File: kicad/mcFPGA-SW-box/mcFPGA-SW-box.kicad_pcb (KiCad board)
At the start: 4 copper layers, 120 parts, among them J1 Conn_01x04, J10 Conn_01x02, J11 Conn_01x02, J12 Conn_01x02, J2 Conn_01x04, J3 Conn_01x04, J4 Conn_01x04, J5 Conn_01x04, J6 Conn_01x04, J7 Conn_01x04, J8 Conn_01x02, J9 Conn_01x04, U1 74HC595, U10 NC7SB3157P6X, U11 NC7SB3157P6X, U12 NC7SB3157P6X, U13 NC7SB3157P6X, U14 NC7SB3157P6X, U15 NC7SB3157P6X, U16 NC7SB3157P6X, U17 NC7SB3157P6X, U18 NC7SB3157P6X, U19 NC7SB3157P6X, U2 74HC595, U20 NC7SB3157P6X, U21 NC7SB3157P6X, U22 NC7SB3157P6X, U23 NC7SB3157P6X, U24 NC7SB3157P6X, U25 NC7SB3157P6X, U26 NC7SB3157P6X, U27 NC7SB3157P6X, U28 NC7SB3157P6X, U29 NC7SB3157P6X, U3 74HC595, U30 NC7SB3157P6X, U31 NC7SB3157P6X, U32 NC7SB3157P6X, U33 NC7SB3157P6X, U34 NC7SB3157P6X, U35 NC7SB3157P6X, U36 NC7SB3157P6X, U4 74HC595, U5 NC7SB3157P6X, U6 NC7SB3157P6X, U7 NC7SB3157P6X, U8 NC7SB3157P6X, U9 NC7SB3157P6X

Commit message: start layout of SW box
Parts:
- moved D25 240.0 mm to (114.3, 88.9)
- moved D26 238.8 mm to (114.3, 83.8)
- moved D27 237.9 mm to (114.3, 78.7)
- moved U4 237.3 mm to (114.3, 43.7)
- moved D28 237.2 mm to (114.3, 73.7)
- moved U3 235.4 mm to (114.3, 97.3)
- moved D21 232.3 mm to (114.3, 66.0)
- moved D22 232.3 mm to (114.3, 61.0)
- moved D12 220.9 mm to (124.5, 96.5)
- moved D16 218.4 mm to (124.5, 53.3)
- moved D11 214.0 mm to (132.1, 96.5)
- moved D15 210.6 mm to (132.1, 53.3)
- moved D10 207.1 mm to (139.7, 96.5)
- moved J2 206.2 mm to (97.8, 46.0), turned to 180 degrees
- moved D14 202.8 mm to (139.7, 53.3)
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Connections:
- J12 pad 2: /prio_east_0 -> unconnected-(J12-Pin_2-Pad2)
- U25 pad 1: Net-(U25-Pad1) -> /prio_west_1
- U25 pad 4: /prio_west_1 -> Net-(U25-Pad4)
- U26 pad 1: Net-(U26-Pad1) -> /prio_west_0
- U26 pad 4: /prio_west_0 -> Net-(U26-Pad4)
- U28 pad 4: Net-(U25-Pad1) -> Net-(U25-Pad4)
- U29 pad 4: Net-(U26-Pad1) -> Net-(U26-Pad4)
- U32 pad 4: Net-(U25-Pad1) -> Net-(U25-Pad4)
- U33 pad 4: Net-(U26-Pad1) -> Net-(U26-Pad4)
- U35 pad 4: Net-(U25-Pad1) -> Net-(U25-Pad4)
- U36 pad 4: Net-(U26-Pad1) -> Net-(U26-Pad4)
- U5 pad 1: Net-(U21-Pad4) -> unconnected-(U5-Pad1)
- U5 pad 3: unconnected-(U5-Pad3) -> /west_3
- U5 pad 4: /west_3 -> Net-(U21-Pad4)
- U6 pad 1: Net-(U12-Pad4) -> unconnected-(U6-Pad1)
- U6 pad 3: unconnected-(U6-Pad3) -> /west_2
- U6 pad 4: /west_2 -> Net-(U12-Pad4)
- U7 pad 1: Net-(U15-Pad4) -> unconnected-(U7-Pad1)
- U7 pad 3: unconnected-(U7-Pad3) -> /west_1
- U7 pad 4: /west_1 -> Net-(U15-Pad4)
- U8 pad 1: Net-(U18-Pad4) -> unconnected-(U8-Pad1)
- U8 pad 3: unconnected-(U8-Pad3) -> /west_0
- U8 pad 4: /west_0 -> Net-(U18-Pad4)
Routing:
- net sw_19: track 0.00 -> 77.9 mm, vias 0 -> 2
- net sw_28: track 0.00 -> 76.2 mm, vias 0 -> 1
- net sw_18: track 0.00 -> 73.8 mm, vias 0 -> 2
- net GND: track 70.9 -> 141.8 mm, vias 16 -> 32
- net sw_17: track 0.00 -> 69.1 mm, vias 0 -> 2
- net sw_29: track 0.00 -> 66.0 mm, vias 0 -> 1
- net sw_16: track 0.00 -> 63.7 mm, vias 0 -> 2
- net sw_25: track 0.00 -> 62.5 mm, vias 0 -> 3
- net Net-(U25-Pad4): track 0.00 -> 62.3 mm, vias 0 -> 4
- net Net-(U26-Pad4): track 0.00 -> 61.7 mm, vias 0 -> 4
- net Net-(U12-Pad4): track 0.00 -> 60.7 mm, vias 0 -> 3
- net Net-(U21-Pad4): track 0.00 -> 60.7 mm, vias 0 -> 3
- net Net-(U15-Pad4): track 0.00 -> 60.7 mm, vias 0 -> 3
- net Net-(U18-Pad4): track 0.00 -> 60.7 mm, vias 0 -> 3
- net sw_24: track 0.00 -> 53.7 mm, vias 0 -> 1
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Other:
- board outline added: 100 x 85 mm

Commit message: SWbox layout nearly complete
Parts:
- moved C4 105.6 mm to (114.3, 41.9), turned to 180 degrees
- moved C1 77.2 mm to (114.3, 92.7), turned to 180 degrees
- moved C3 73.1 mm to (172.7, 41.9), turned to 180 degrees
- moved C6 61.1 mm to (110.5, 127.6)
- moved C8 61.1 mm to (110.5, 130.9)
- moved C5 61.1 mm to (106.4, 128.1)
- moved C7 61.1 mm to (106.4, 130.7)
- moved J3 40.5 mm to (99.0, 67.6)
- moved J4 40.0 mm to (150.0, 110.0)
- moved J11 39.5 mm to (160.0, 110.0)
- moved J8 36.6 mm to (99.0, 52.5)
- moved C2 24.8 mm to (172.7, 92.7), turned to 180 degrees
- moved J7 20.2 mm to (99.0, 108.0)
- moved J9 19.9 mm to (185.0, 100.4)
- moved J6 17.6 mm to (185.0, 60.0)
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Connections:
- J1 pad 1: GND -> SCLK
- J1 pad 2: LATCH -> MOSI
- J1 pad 3: MOSI -> LATCH
- J1 pad 4: SCLK -> GND
- J12 pad 2: unconnected-(J12-Pin_2-Pad2) -> /prio_east_0
- U5 pad 1: unconnected-(U5-Pad1) -> /west_3
- U5 pad 3: /west_3 -> unconnected-(U5-Pad3)
- U6 pad 1: unconnected-(U6-Pad1) -> /west_2
- U6 pad 3: /west_2 -> unconnected-(U6-Pad3)
- U7 pad 1: unconnected-(U7-Pad1) -> /west_1
- U7 pad 3: /west_1 -> unconnected-(U7-Pad3)
- U8 pad 1: unconnected-(U8-Pad1) -> /west_0
- U8 pad 3: /west_0 -> unconnected-(U8-Pad3)
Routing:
- net LATCH: track 0.00 -> 229.6 mm, vias 0 -> 9
- net SCLK: track 0.00 -> 221.0 mm, vias 0 -> 7
- net sw_12: track 4.28 -> 95.0 mm, vias 1 -> 2
- net sw_13: track 4.28 -> 88.4 mm, vias 1 -> 2
- net sw_14: track 4.28 -> 81.6 mm, vias 1 -> 2
- net xp_0: track 4.20 -> 77.8 mm, vias 1 -> 3
- net xp_4: track 4.13 -> 76.9 mm, vias 1 -> 4
- net sw_15: track 4.28 -> 75.0 mm, vias 1 -> 2
- net Net-(U2-QH'): track 0.00 -> 70.6 mm, vias 0 -> 2
- net Net-(U3-QH'): track 0.00 -> 69.5 mm, vias 0 -> 2
- net xp_1: track 4.13 -> 72.1 mm, vias 1 -> 3
- net xp_5: track 4.13 -> 67.6 mm, vias 1 -> 4
- net xp_6: track 4.39 -> 67.1 mm, vias 1 -> 4
- net GND: track 141.8 -> 199.1 mm, vias 32 -> 38
- net xp_7: track 4.13 -> 60.2 mm, vias 1 -> 4
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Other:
- board size 100 x 85 mm -> 100 x 100 mm

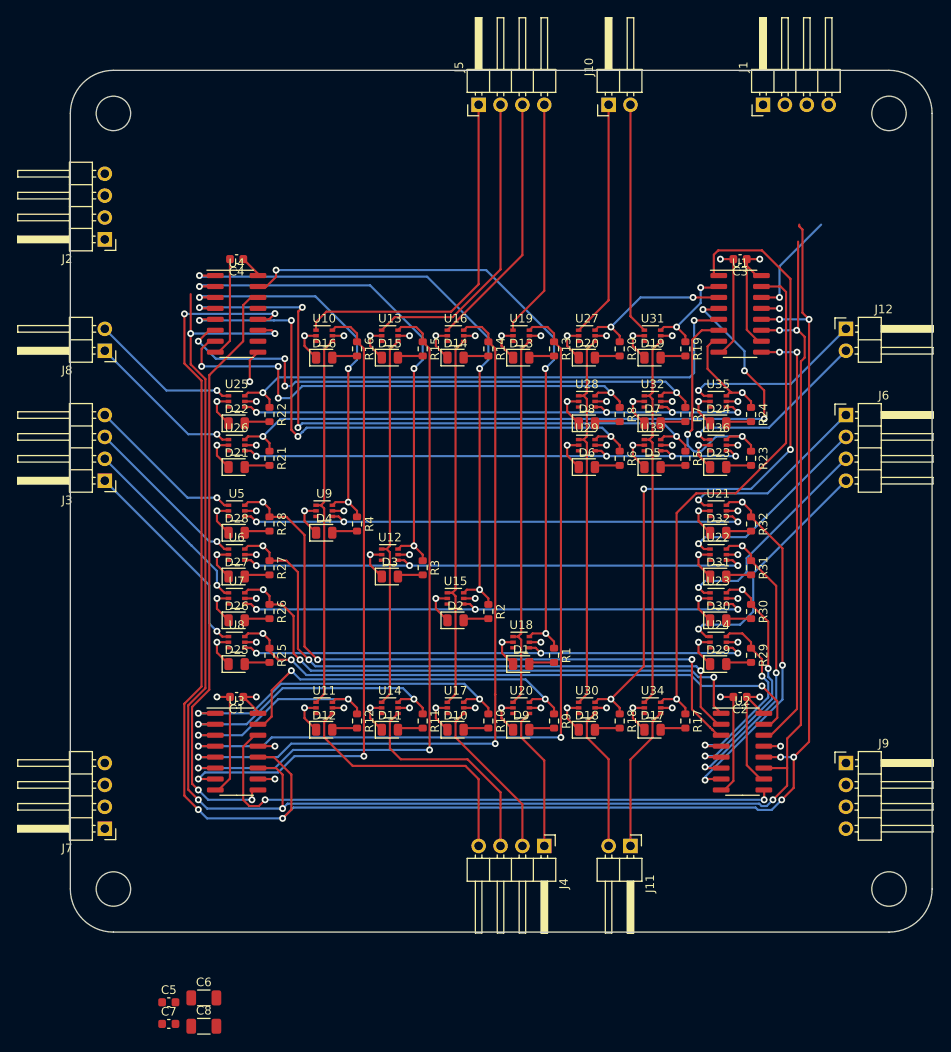
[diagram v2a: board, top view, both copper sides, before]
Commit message: sw box layout almost complete
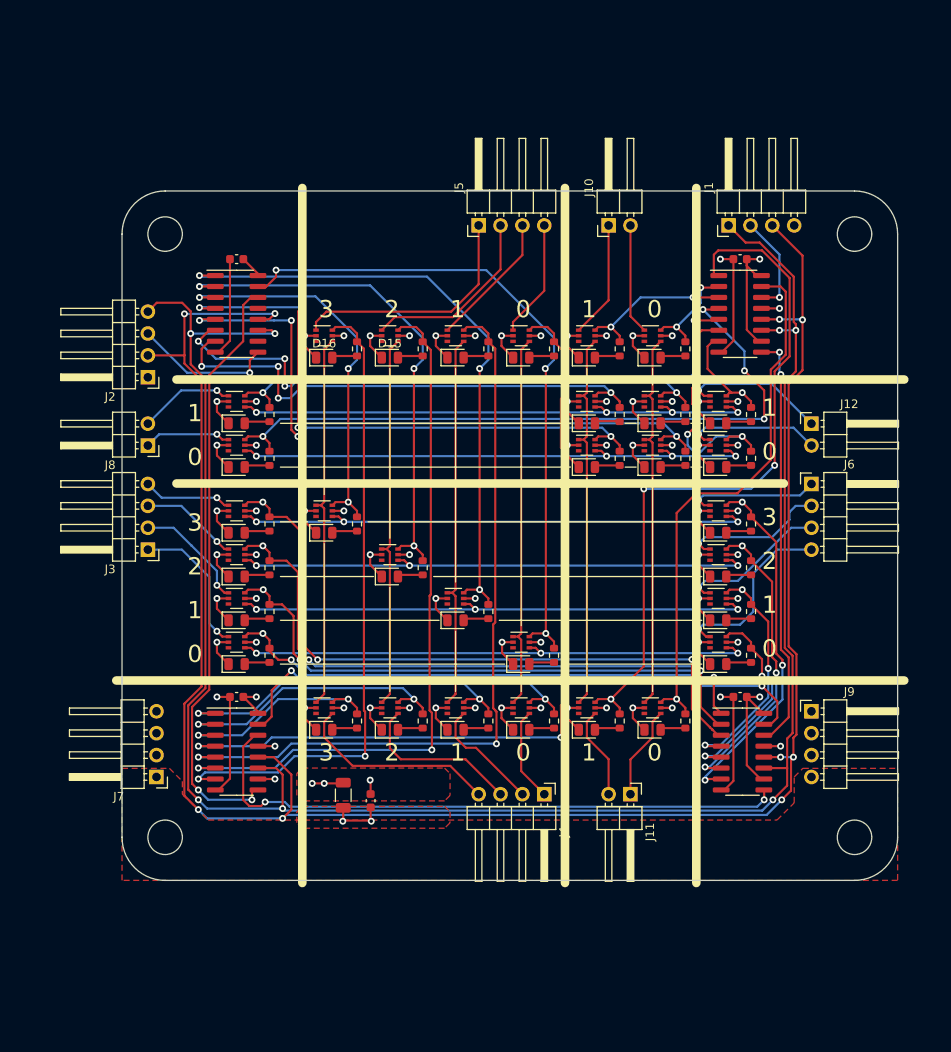
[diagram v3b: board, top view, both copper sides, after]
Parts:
- removed C7: 100n, Capacitor_SMD:C_0603_1608Metric
- removed C8: 22u, Resistor_SMD:R_1206_3216Metric
- moved C5 33.1 mm to (129.8, 104.8), turned to -90 degrees
- moved C6 28.5 mm to (126.7, 104.1), turned to -90 degrees
- moved J2 16.8 mm to (104.0, 55.6)
- moved J1 14.6 mm to (171.4, 38.0)
- moved J10 14.0 mm to (157.5, 38.0)
- moved J5 14.0 mm to (142.4, 38.0)
- moved J8 12.1 mm to (104.0, 63.5)
- moved J12 11.7 mm to (181.0, 61.0)
- moved J3 9.43 mm to (104.0, 75.6)
- moved J6 8.94 mm to (181.0, 68.0)
- moved J7 8.49 mm to (105.0, 102.0)
- moved J9 7.21 mm to (181.0, 94.4)
- moved J11 6.00 mm to (160.0, 104.0)
- moved J4 6.00 mm to (150.0, 104.0)
- renumbered R17 to Re
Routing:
- net /north_2: track 35.8 -> 21.8 mm
- net /north_1: track 29.8 -> 15.8 mm
- net /north_0: track 27.7 -> 13.7 mm
- net /prio_north_1: track 27.6 -> 13.6 mm
- net /prio_north_0: track 26.9 -> 12.9 mm
- net /north_3: track 42.4 -> 28.4 mm
- net MISO: track 3.82 -> 16.5 mm
- net SCLK: track 221.0 -> 230.6 mm
- net /prio_west_0: track 18.6 -> 10.1 mm
- net /west_1: track 21.8 -> 13.5 mm
- net /west_3: track 18.7 -> 10.4 mm
- net /west_2: track 19.7 -> 11.4 mm
- net /east_1: track 25.8 -> 17.6 mm
- net /west_0: track 24.5 -> 16.7 mm
- net /east_0: track 28.5 -> 21.2 mm
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- added copper zone on F.Cu, net +3.3VP
- added copper zone on In2.Cu, net +3.3VP
- added copper zone on F.Cu, net +3V3
- added copper zone on F.Cu, net GND
- added copper zone on In1.Cu, net GND
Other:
- board size 100 x 100 mm -> 90 x 80 mm
- board text added: "0"
- board text added: "1"
- board text added: "2"
- board text added: "3"
